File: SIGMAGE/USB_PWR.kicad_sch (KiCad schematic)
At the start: 45 parts, among them J1 UJ31CHG2SMTTR, J14 HTSW10807GD, J15 HTSW10807GD, J16 HTSW10807GD, J17 HTSW10807GD, J18 HTSW10107GD, J19 HTSW10107GD, J20 HTSW10107GD, U1 MAX8902BATA/V+T, U2 MAX8902BATA/V+T, U3 MAX8902BATA/V+T

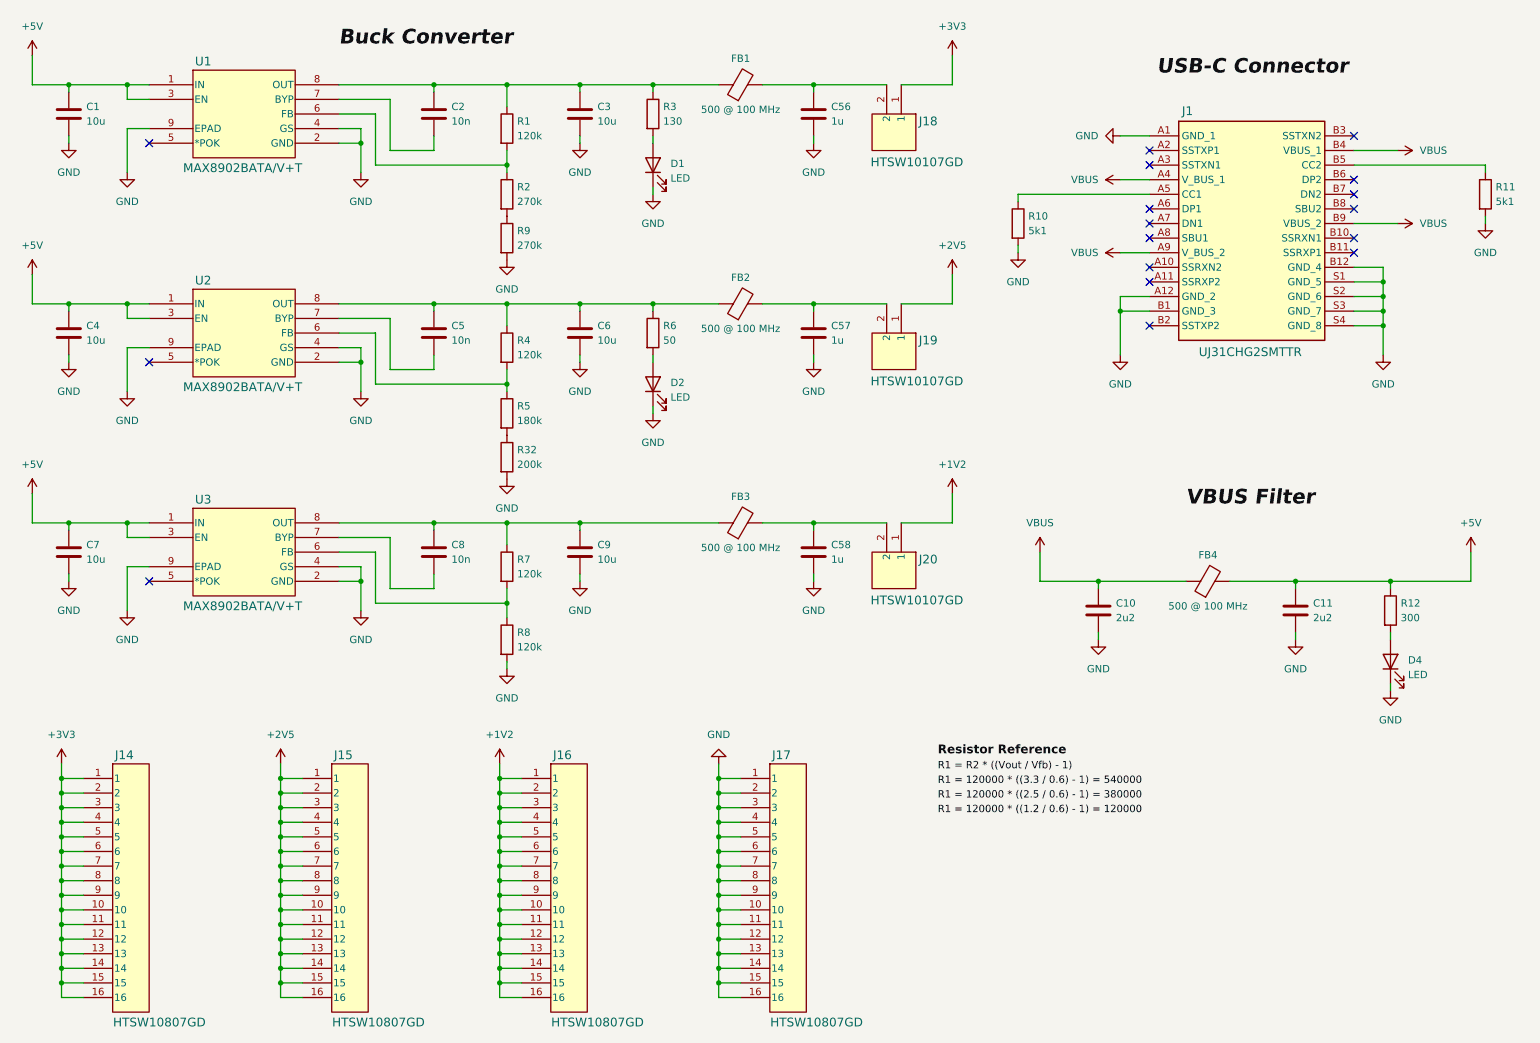
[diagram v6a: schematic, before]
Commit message: Makin it waaay cheaper and JLCPCB conform
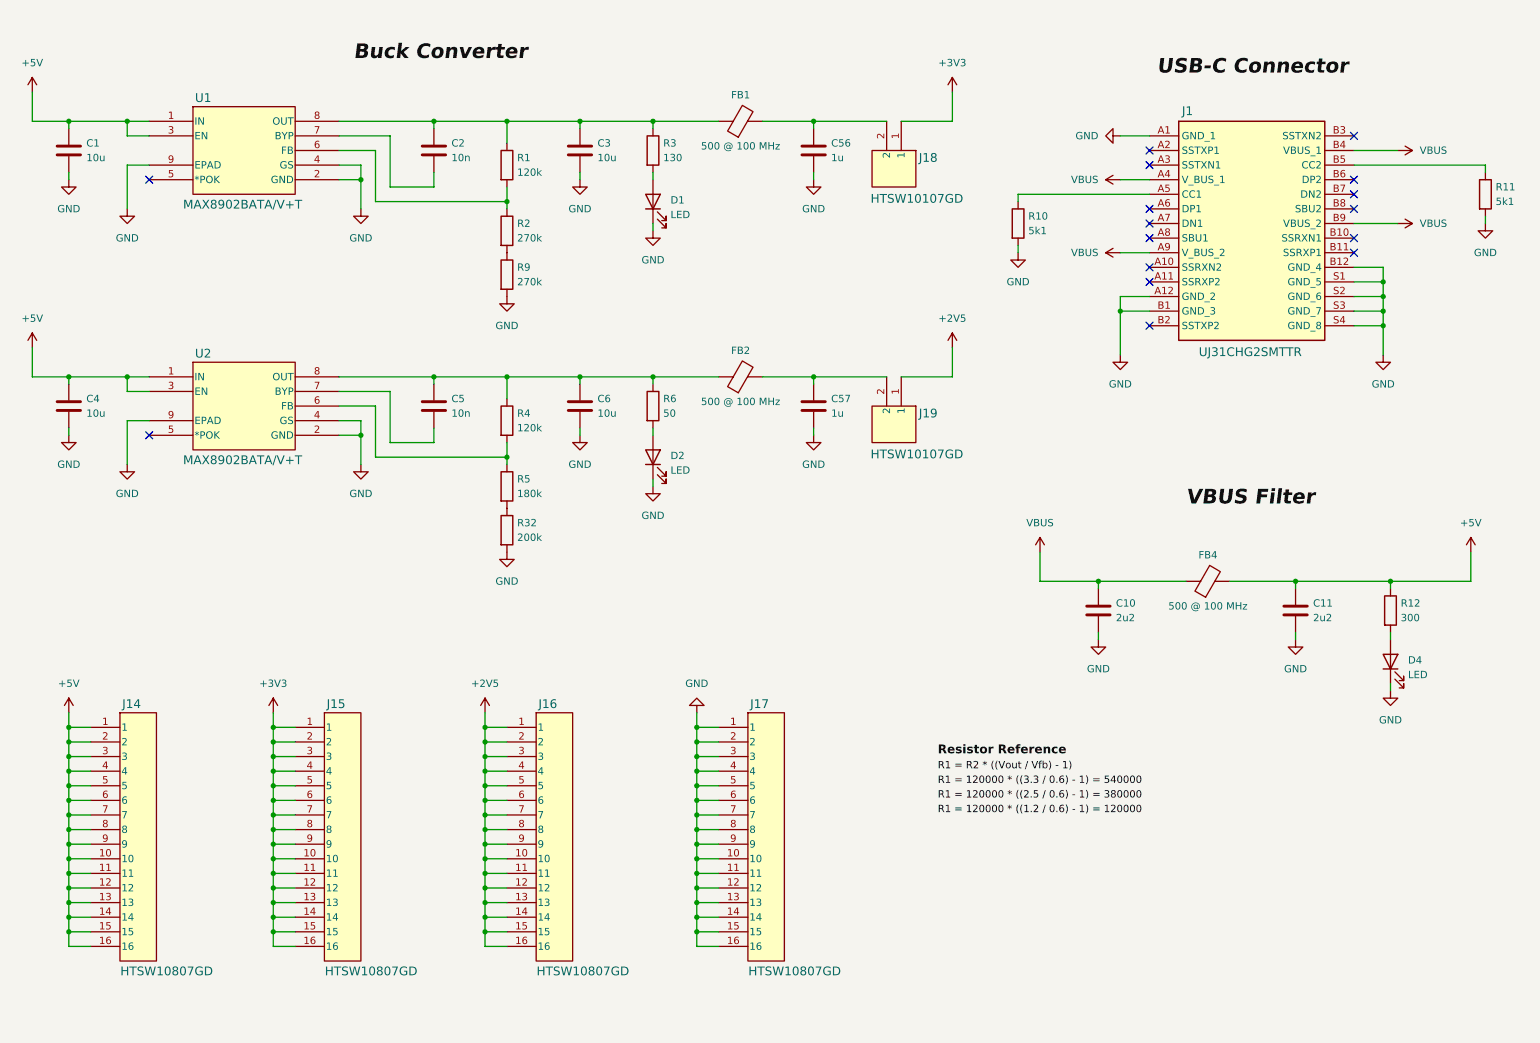
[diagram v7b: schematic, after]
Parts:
- removed C58: 1u, Capacitor_SMD:C_0603_1608Metric, symbol Device:C
- removed C7, C9: 10u, Capacitor_SMD:C_0603_1608Metric, symbol Device:C
- removed C8: 10n, Capacitor_SMD:C_0603_1608Metric, symbol Device:C
- removed FB3: 500 @ 100 MHz, Capacitor_SMD:C_0603_1608Metric, symbol Device:FerriteBead
- removed J20: HTSW10107GD, SIGMAGE:HTSW10107GD, symbol SIGMAGE:HTSW10107GD
- removed R7, R8: 120k, Resistor_SMD:R_0603_1608Metric, symbol Device:R
- removed U3: MAX8902BATA/V+T, SIGMAGE:MAX8902BATAVT, symbol SIGMAGE:MAX8902BATAVT
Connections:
- net +1V2 is gone; now on net +2V5: J16.1, J16.10, J16.11, J16.12, J16.13, J16.14, J16.15, J16.16, J16.2, J16.3, J16.4, J16.5, J16.6, J16.7, J16.8, J16.9
- net +2V5: no longer J15.1, J15.10, J15.11, J15.12, J15.13, J15.14, J15.15, J15.16, J15.2, J15.3, J15.4, J15.5, J15.6, J15.7, J15.8, J15.9
- net +3V3: now also J15.1, J15.10, J15.11, J15.12, J15.13, J15.14, J15.15, J15.16, J15.2, J15.3, J15.4, J15.5, J15.6, J15.7, J15.8, J15.9; no longer J14.1, J14.10, J14.11, J14.12, J14.13, J14.14, J14.15, J14.16, J14.2, J14.3, J14.4, J14.5, J14.6, J14.7, J14.8, J14.9
- net +5V: now also J14.1, J14.10, J14.11, J14.12, J14.13, J14.14, J14.15, J14.16, J14.2, J14.3, J14.4, J14.5, J14.6, J14.7, J14.8, J14.9
- no-connect marks 17 -> 16
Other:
- moved on the sheet: C1, C2, C3, C4, C5, C56, C57, C6, D1, D2, FB1, FB2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
